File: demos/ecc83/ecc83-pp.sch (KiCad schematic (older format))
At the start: 11 parts, among them P1 IN, P2 OUT, P3 POWER, P4 CONN_2, U1 ECC83

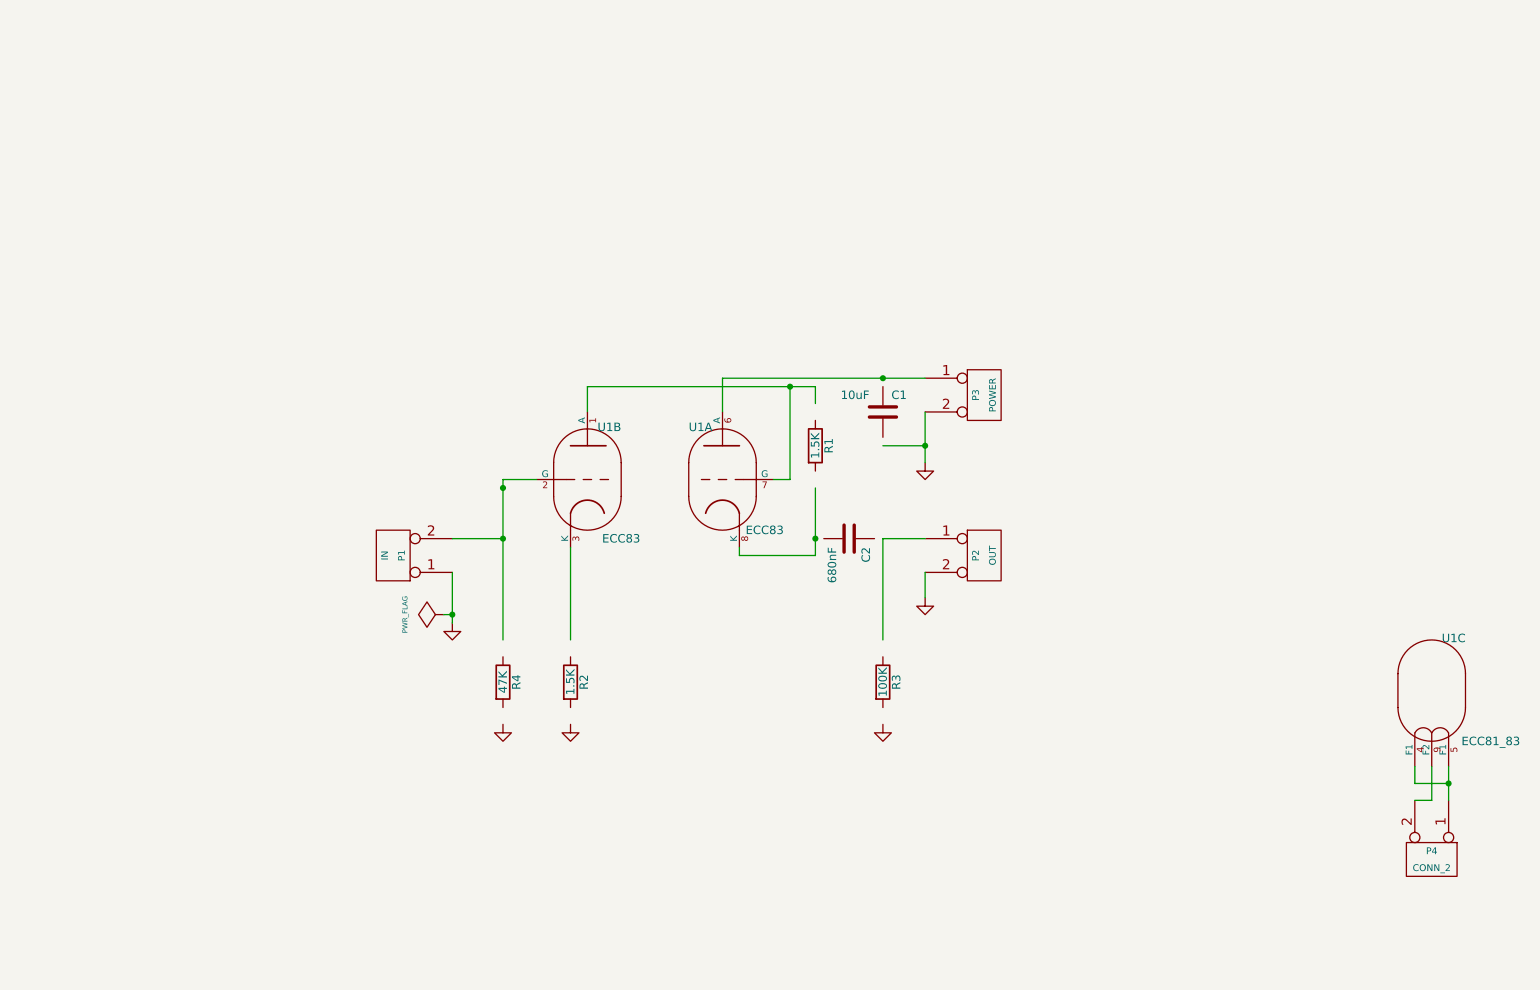
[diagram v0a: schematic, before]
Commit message: Update old demo board files. Minor code cleaning.
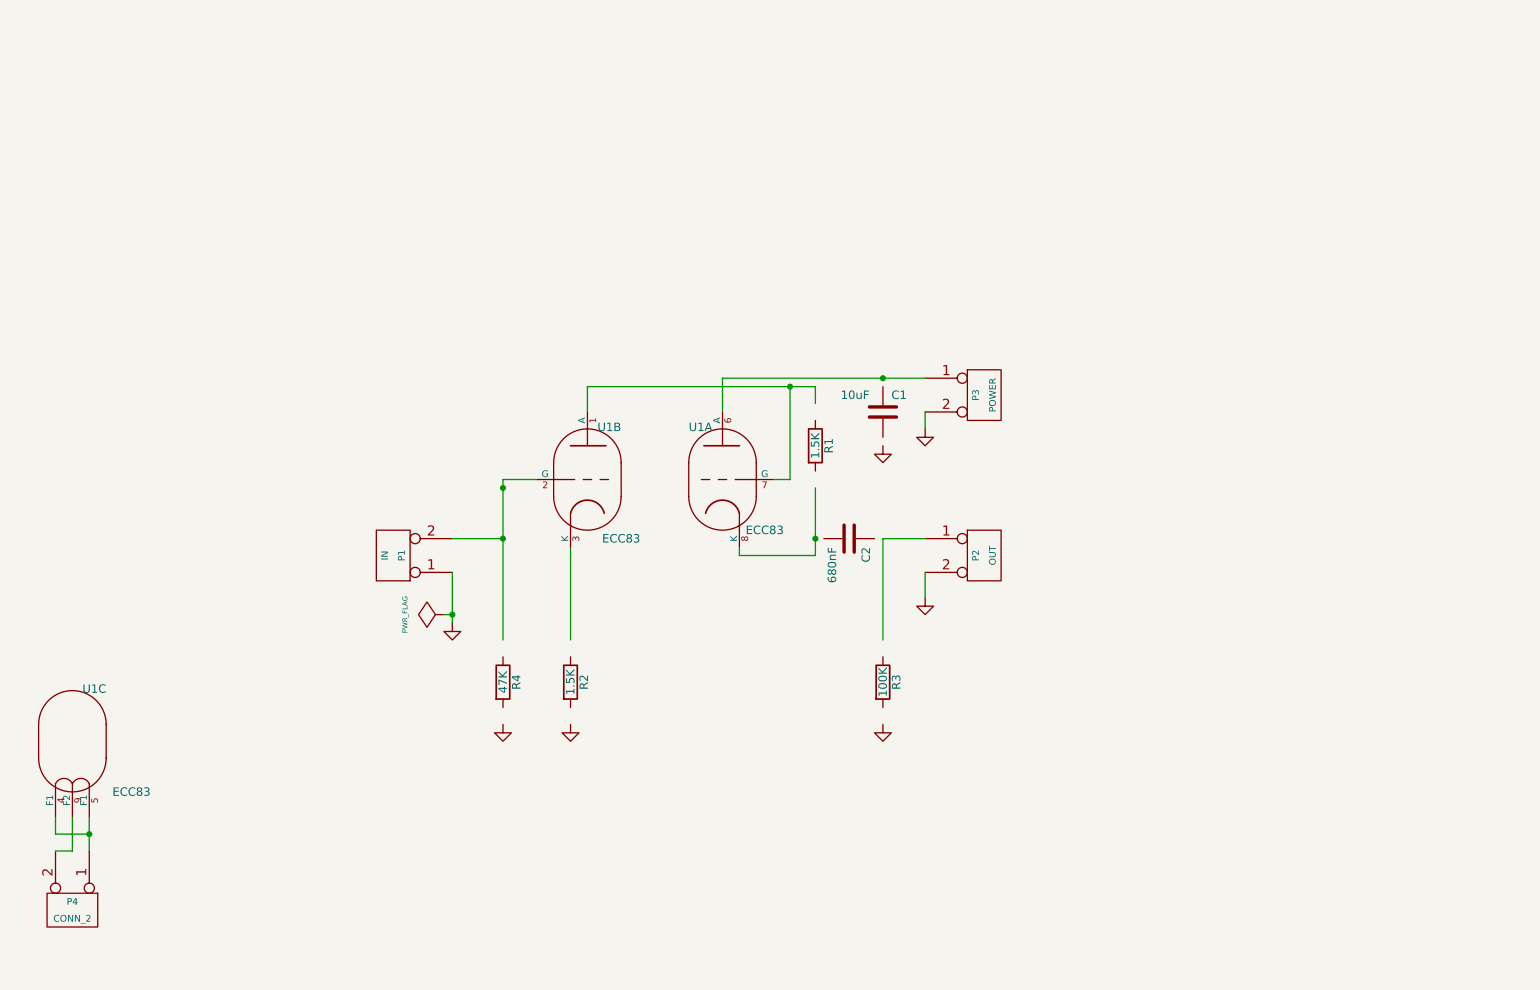
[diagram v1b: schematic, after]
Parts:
- U1: value ECC81_83 -> ECC83
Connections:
- wire segments 26 -> 25
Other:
- moved on the sheet: P4, U1C
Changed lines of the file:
@@
 EESchema Schematic File Version 2
-LIBS:power,device,conn,valves,linear,regul,74xx,cmos4000,adc-dac,memory,xilinx,special,microcontrollers,microchip,analog_switches,motorola,intel,audio,interface,digital-audio,philips,display,cypress,siliconi,contrib,.\ecc83-pp.cache
-EELAYER 23  0
+LIBS:power
+LIBS:device
+LIBS:conn
+LIBS:valves
+LIBS:linear
+LIBS:regul
+LIBS:74xx
+LIBS:cmos4000
+LIBS:adc-dac
+LIBS:memory
+LIBS:xilinx
+LIBS:special
+LIBS:microcontrollers
+LIBS:microchip
+LIBS:analog_switches
+LIBS:motorola
+LIBS:intel
+LIBS:audio
+LIBS:interface
+LIBS:digital-audio
+LIBS:philips
+LIBS:display
+LIBS:cypress
+LIBS:siliconi
+LIBS:contrib
+EELAYER 24 0
 EELAYER END
-$Descr A4 11700 8267
+$Descr A4 11693 8268
+encoding utf-8
 Sheet 1 1
 Title "ECC Push-Pull"
-Date "11 dec 2006"
+Date "vendredi 04 juillet 2014"
 Rev "0.1"
 Comp ""
@@
 Connection ~ 4450 4500
 Wire Wire Line
-	4450 5400 4450 4450
+	4450 4450 4450 5400
 Wire Wire Line
 	4450 4450 4650 4450
 Wire Wire Line
-	9850 6350 9950 6350
-Wire Wire Line
-	9950 6350 9950 6150
-Wire Wire Line
-	4150 5300 4150 5000
+	1800 6650 1900 6650
+Wire Wire Line
+	1900 6650 1900 6450
+Wire Wire Line
+	4150 5000 4150 5300
 Wire Wire Line
 	6950 5150 6950 5000
@@
 Connection ~ 4450 4800
 Wire Wire Line
-	6950 4350 6950 4050
-Connection ~ 6950 4250
+	6950 4150 6950 4050
 Wire Wire Line
 	4850 4850 4850 5400
@@
 	6300 3900 6300 4000
 Wire Wire Line
-	6950 3850 5750 3850
+	5750 3850 6950 3850
 Connection ~ 6700 3850
-Wire Wire Line
-	6700 4250 6950 4250
 Wire Wire Line
 	6150 4450 6150 3900
@@
 	6700 4800 6700 5400
 Wire Wire Line
-	10050 6150 10050 6350
-Wire Wire Line
-	10050 6250 9850 6250
-Connection ~ 10050 6250
+	2000 6450 2000 6650
+Wire Wire Line
+	2000 6550 1800 6550
+Connection ~ 2000 6550
 Wire Wire Line
 	4100 5250 4150 5250
 Connection ~ 4150 5250
 Wire Wire Line
-	9850 6250 9850 6150
-Wire Wire Line
-	6300 3900 4950 3900
+	1800 6550 1800 6450
+Wire Wire Line
+	4950 3900 6300 3900
 Wire Wire Line
 	4950 3900 4950 4050
@@
 L ECC83 U1
 U 3 1 48B4F266
-P 9950 5700
-F 0 "U1" H 10080 6010 50  0000 C C
-F 1 "ECC81_83" H 10300 5400 50  0000 C C
-F 2 "VALVE-NOVAL_P" H 10220 5300 50  0001 C C
-	3    9950 5700
+P 1900 6000
+F 0 "U1" H 2030 6310 50  0000 C CNN
+F 1 "ECC83" H 2250 5700 50  0000 C CNN
+F 2 "VALVE-NOVAL_P" H 2170 5600 50  0001 C CNN
+F 3 "" H 1900 6000 60  0001 C CNN
+	3    1900 6000
 	1    0    0    -1
 $EndComp
@@
 U 2 1 48B4F263
 P 4950 4450
-F 0 "U1" H 5080 4760 50  0000 C C
-F 1 "ECC83" H 5150 4100 50  0000 C C
-F 2 "VALVE-NOVAL_P" H 5220 4050 50  0001 C C
+F 0 "U1" H 5080 4760 50  0000 C CNN
+F 1 "ECC83" H 5150 4100 50  0000 C CNN
+F 2 "VALVE-NOVAL_P" H 5220 4050 50  0001 C CNN
+F 3 "" H 4950 4450 60  0001 C CNN
 	2    4950 4450
 	1    0    0    -1
@@
 U 1 1 48B4F256
 P 5750 4450
-F 0 "U1" H 5880 4760 50  0000 C C
-F 1 "ECC83" H 5500 4150 50  0000 C C
-F 2 "VALVE-NOVAL_P" H 6020 4050 50  0001 C C
+F 0 "U1" H 5880 4760 50  0000 C CNN
+F 1 "ECC83" H 5500 4150 50  0000 C CNN
+F 2 "VALVE-NOVAL_P" H 6020 4050 50  0001 C CNN
+F 3 "" H 5750 4450 60  0001 C CNN
 	1    5750 4450
 	-1   0    0    -1
@@
 U 1 1 457DBAF8
 P 6950 5150
-F 0 "#PWR01" H 6950 5150 30  0001 C C
-F 1 "GND" H 6950 5080 30  0001 C C
+F 0 "#PWR01" H 6950 5150 30  0001 C CNN
+F 1 "GND" H 6950 5080 30  0001 C CNN
+F 2 "" H 6950 5150 60  0001 C CNN
+F 3 "" H 6950 5150 60  0001 C CNN
 	1    6950 5150
 	1    0    0    -1
@@
 U 1 1 457DBAF5
 P 6700 5900
-F 0 "#PWR02" H 6700 5900 30  0001 C C
-F 1 "GND" H 6700 5830 30  0001 C C
+F 0 "#PWR02" H 6700 5900 30  0001 C CNN
+F 1 "GND" H 6700 5830 30  0001 C CNN
+F 2 "" H 6700 5900 60  0001 C CNN
+F 3 "" H 6700 5900 60  0001 C CNN
 	1    6700 5900
 	1    0    0    -1
@@
 U 1 1 457DBAF1
 P 4850 5900
-F 0 "#PWR03" H 4850 5900 30  0001 C C
-F 1 "GND" H 4850 5830 30  0001 C C
+F 0 "#PWR03" H 4850 5900 30  0001 C CNN
+F 1 "GND" H 4850 5830 30  0001 C CNN
+F 2 "" H 4850 5900 60  0001 C CNN
+F 3 "" H 4850 5900 60  0001 C CNN
 	1    4850 5900
 	1    0    0    -1
@@
 U 1 1 457DBAEF
 P 4450 5900
-F 0 "#PWR04" H 4450 5900 30  0001 C C
-F 1 "GND" H 4450 5830 30  0001 C C
+F 0 "#PWR04" H 4450 5900 30  0001 C CNN
+F 1 "GND" H 4450 5830 30  0001 C CNN
+F 2 "" H 4450 5900 60  0001 C CNN
+F 3 "" H 4450 5900 60  0001 C CNN
 	1    4450 5900
 	1    0    0    -1
@@
 U 1 1 457DBAC0
 P 4100 5250
-F 0 "#FLG05" H 4100 5520 30  0001 C C
-F 1 "PWR_FLAG" H 4100 5480 30  0000 C C
+F 0 "#FLG05" H 4100 5520 30  0001 C CNN
+F 1 "PWR_FLAG" H 4100 5480 30  0000 C CNN
+F 2 "" H 4100 5250 60  0001 C CNN
+F 3 "" H 4100 5250 60  0001 C CNN
 	1    4100 5250
 	0    -1   -1   0
@@
 L CONN_2 P4
 U 1 1 456A8ACC
-P 9950 6700
-F 0 "P4" V 9900 6700 40  0000 C C
-F 1 "CONN_2" V 10000 6700 40  0000 C C
-	1    9950 6700
+P 1900 7000
+F 0 "P4" V 1850 7000 40  0000 C CNN
+F 1 "CONN_2" V 1950 7000 40  0000 C CNN
+F 2 "" H 1900 7000 60  0001 C CNN
+F 3 "" H 1900 7000 60  0001 C CNN
+	1    1900 7000
 	0    1    1    0
 $EndComp
@@
 U 1 1 4549F4BE
 P 6700 4050
-F 0 "C1" H 6750 4150 50  0000 L C
-F 1 "10uF" H 6450 4150 50  0000 L C
+F 0 "C1" H 6750 4150 50  0000 L CNN
+F 1 "10uF" H 6450 4150 50  0000 L CNN
+F 2 "" H 6700 4050 60  0001 C CNN
+F 3 "" H 6700 4050 60  0001 C CNN
 	1    6700 4050
 	1    0    0    -1
@@
 U 1 1 4549F4B9
 P 4150 5300
-F 0 "#PWR06" H 4150 5300 30  0001 C C
-F 1 "GND" H 4150 5230 30  0001 C C
+F 0 "#PWR06" H 4150 5300 30  0001 C CNN
+F 1 "GND" H 4150 5230 30  0001 C CNN
+F 2 "" H 4150 5300 60  0001 C CNN
+F 3 "" H 4150 5300 60  0001 C CNN
 	1    4150 5300
 	1    0    0    -1
@@
 L GND #PWR07
 U 1 1 4549F4B3
-P 6950 4350
-F 0 "#PWR07" H 6950 4350 30  0001 C C
-F 1 "GND" H 6950 4280 30  0001 C C
-	1    6950 4350
+P 6950 4150
+F 0 "#PWR07" H 6950 4150 30  0001 C CNN
+F 1 "GND" H 6950 4080 30  0001 C CNN
+F 2 "" H 6950 4150 60  0001 C CNN
+F 3 "" H 6950 4150 60  0001 C CNN
+	1    6950 4150
 	1    0    0    -1
 $EndComp
@@
 U 1 1 4549F4A5
 P 7300 3950
-F 0 "P3" V 7250 3950 40  0000 C C
-F 1 "POWER" V 7350 3950 40  0000 C C
+F 0 "P3" V 7250 3950 40  0000 C CNN
+F 1 "POWER" V 7350 3950 40  0000 C CNN
+F 2 "" H 7300 3950 60  0001 C CNN
+F 3 "" H 7300 3950 60  0001 C CNN
 	1    7300 3950
 	1    0    0    -1
@@
 U 1 1 4549F46C
 P 7300 4900
-F 0 "P2" V 7250 4900 40  0000 C C
-F 1 "OUT" V 7350 4900 40  0000 C C
+F 0 "P2" V 7250 4900 40  0000 C CNN
+F 1 "OUT" V 7350 4900 40  0000 C CNN
+F 2 "" H 7300 4900 60  0001 C CNN
+F 3 "" H 7300 4900 60  0001 C CNN
 	1    7300 4900
 	1    0    0    -1
@@
 U 1 1 4549F464
 P 3800 4900
-F 0 "P1" V 3750 4900 40  0000 C C
-F 1 "IN" V 3850 4900 40  0000 C C
+F 0 "P1" V 3750 4900 40  0000 C CNN
+F 1 "IN" V 3850 4900 40  0000 C CNN
+F 2 "" H 3800 4900 60  0001 C CNN
+F 3 "" H 3800 4900 60  0001 C CNN
 	1    3800 4900
 	-1   0    0    1
@@
 U 1 1 4549F3BE
 P 6500 4800
-F 0 "C2" H 6550 4900 50  0000 L C
-F 1 "680nF" H 6550 4700 50  0000 L C
+F 0 "C2" H 6550 4900 50  0000 L CNN
+F 1 "680nF" H 6550 4700 50  0000 L CNN
+F 2 "" H 6500 4800 60  0001 C CNN
+F 3 "" H 6500 4800 60  0001 C CNN
 	1    6500 4800
 	0    1    1    0
@@
 U 1 1 4549F3AD
 P 6700 5650
-F 0 "R3" V 6780 5650 50  0000 C C
-F 1 "100K" V 6700 5650 50  0000 C C
+F 0 "R3" V 6780 5650 50  0000 C CNN
+F 1 "100K" V 6700 5650 50  0000 C CNN
+F 2 "" H 6700 5650 60  0001 C CNN
+F 3 "" H 6700 5650 60  0001 C CNN
 	1    6700 5650
 	1    0    0    -1
@@
 U 1 1 4549F3A2
 P 4450 5650
-F 0 "R4" V 4530 5650 50  0000 C C
-F 1 "47K" V 4450 5650 50  0000 C C
+F 0 "R4" V 4530 5650 50  0000 C CNN
+F 1 "47K" V 4450 5650 50  0000 C CNN
+F 2 "" H 4450 5650 60  0001 C CNN
+F 3 "" H 4450 5650 60  0001 C CNN
 	1    4450 5650
 	1    0    0    -1
@@
 U 1 1 4549F39D
 P 4850 5650
-F 0 "R2" V 4930 5650 50  0000 C C
-F 1 "1.5K" V 4850 5650 50  0000 C C
+F 0 "R2" V 4930 5650 50  0000 C CNN
+F 1 "1.5K" V 4850 5650 50  0000 C CNN
+F 2 "" H 4850 5650 60  0001 C CNN
+F 3 "" H 4850 5650 60  0001 C CNN
 	1    4850 5650
 	1    0    0    -1
@@
 U 1 1 4549F38A
 P 6300 4250
-F 0 "R1" V 6380 4250 50  0000 C C
-F 1 "1.5K" V 6300 4250 50  0000 C C
+F 0 "R1" V 6380 4250 50  0000 C CNN
+F 1 "1.5K" V 6300 4250 50  0000 C CNN
+F 2 "" H 6300 4250 60  0001 C CNN
+F 3 "" H 6300 4250 60  0001 C CNN
 	1    6300 4250
 	1    0    0    -1
 $EndComp
+$Comp
+L GND #PWR08
+U 1 1 53B6F370
+P 6700 4250
+F 0 "#PWR08" H 6700 4250 30  0001 C CNN
+F 1 "GND" H 6700 4180 30  0001 C CNN
+F 2 "" H 6700 4250 60  0001 C CNN
+F 3 "" H 6700 4250 60  0001 C CNN
+	1    6700 4250
+	1    0    0    -1
+$EndComp

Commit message: Update ecc83 demo. default KISYS3DMOD definition on Linux: add /usr/local/kicad/share/kicad/module/package3d test to find a suitable value.
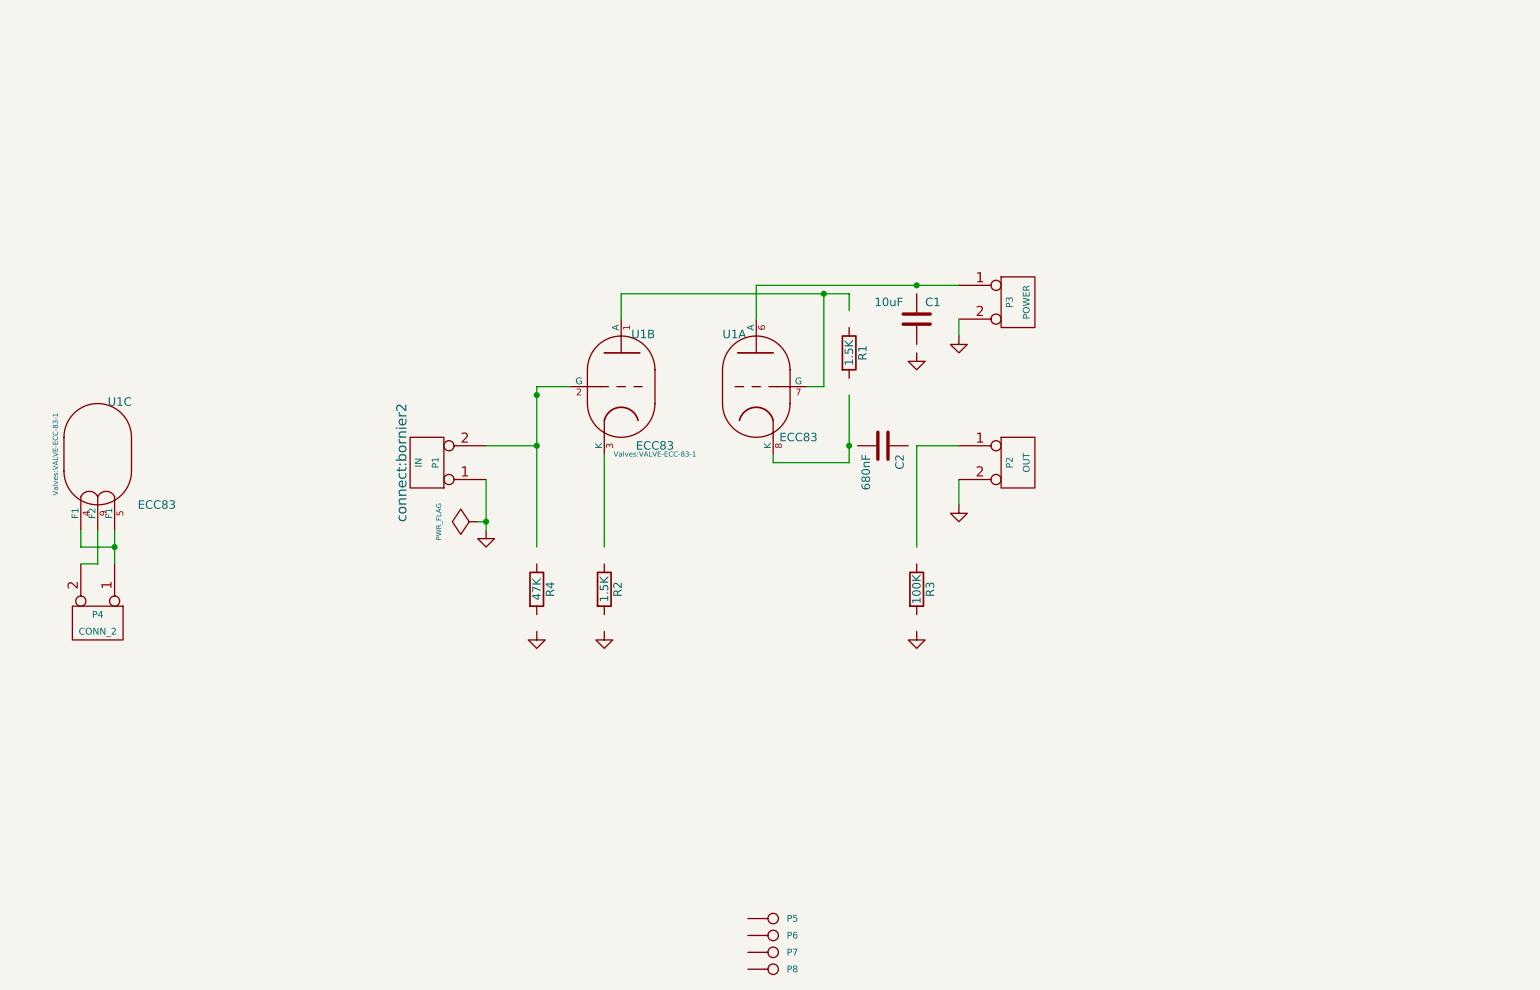
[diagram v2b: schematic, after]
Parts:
- added P5, P6, P7, P8: CONN_1, connect:1pin, symbol CONN_1
- C1: footprint (none) -> discret:C2V10
- C2: footprint (none) -> discret:C2
- P1, P2, P3, P4: footprint (none) -> connect:bornier2
- R1, R2, R3, R4: footprint (none) -> discret:R3
- U1: footprint VALVE-NOVAL_P -> Valves:VALVE-ECC-83-1
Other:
- moved on the sheet: C1, C2, P1, P2, P3, P4, R1, R2, R3, R4, U1A, U1B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

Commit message: demos/ schematic tidying
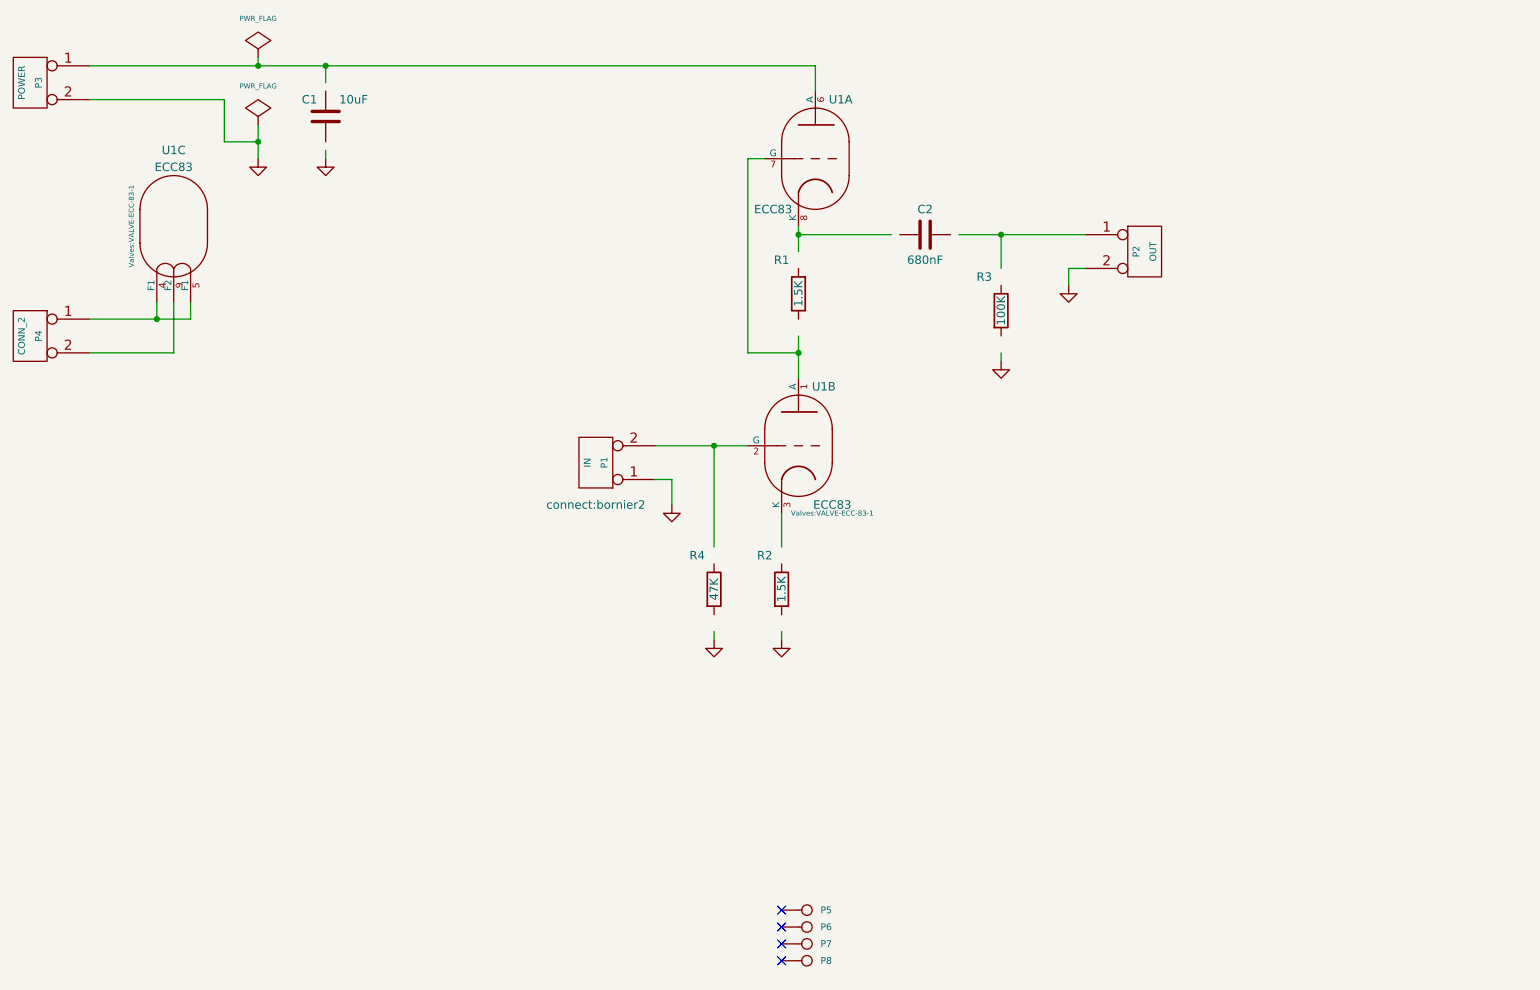
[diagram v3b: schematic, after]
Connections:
- wire segments 25 -> 32
- no-connect marks 0 -> 4
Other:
- moved on the sheet: C1, C2, P1, P2, P3, P4, P5, P6, P7, P8, R1, R2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
